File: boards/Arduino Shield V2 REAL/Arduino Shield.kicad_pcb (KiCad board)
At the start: 2 copper layers, 115 x 75 mm, 22 parts, among them J1 Screw_Terminal_01x07, J11 Screw_Terminal_01x08, J2 Screw_Terminal_01x08, J3 Screw_Terminal_01x08, J4 Screw_Terminal_01x08, J5 Screw_Terminal_01x08, J6 Screw_Terminal_01x08, J7 Screw_Terminal_01x08, J8 Screw_Terminal_01x07, J9 Screw_Terminal_01x10, U1 A000062

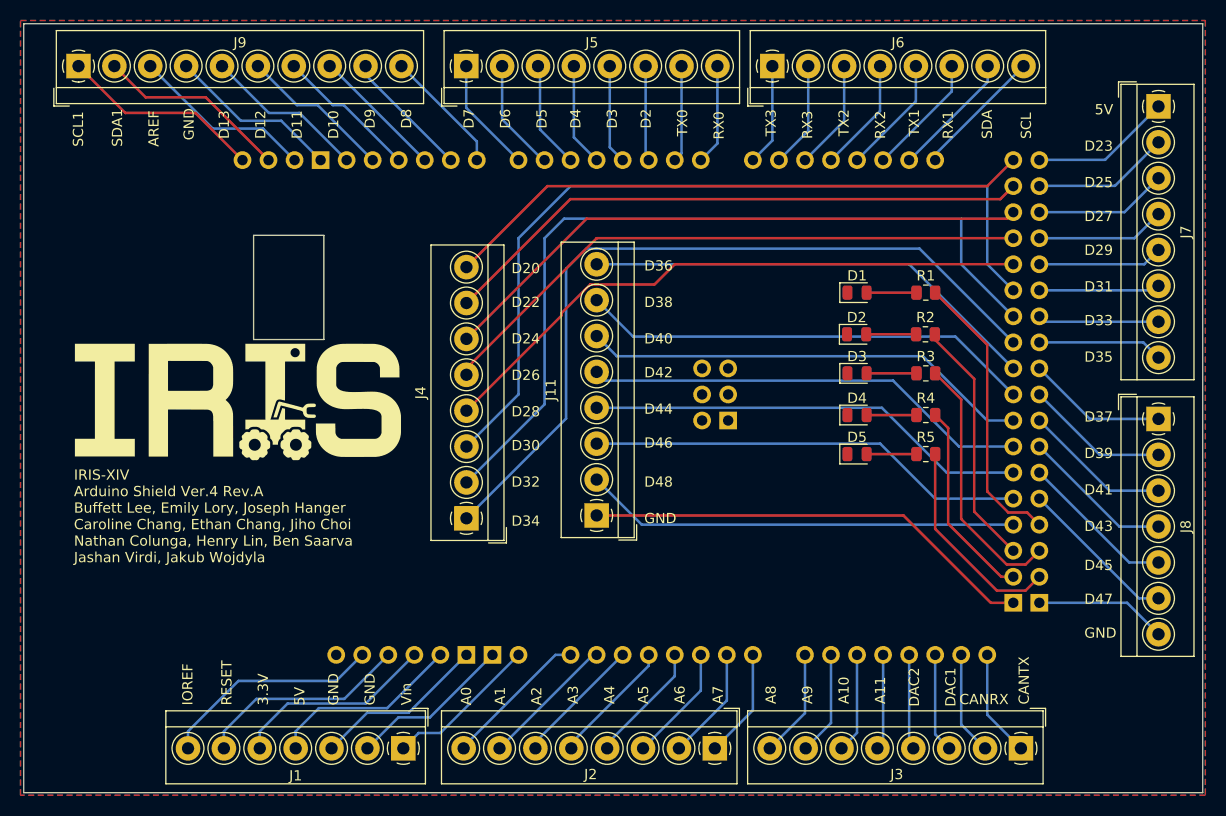
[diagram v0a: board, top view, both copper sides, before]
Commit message: Added LED labels and updated terminal block footprints
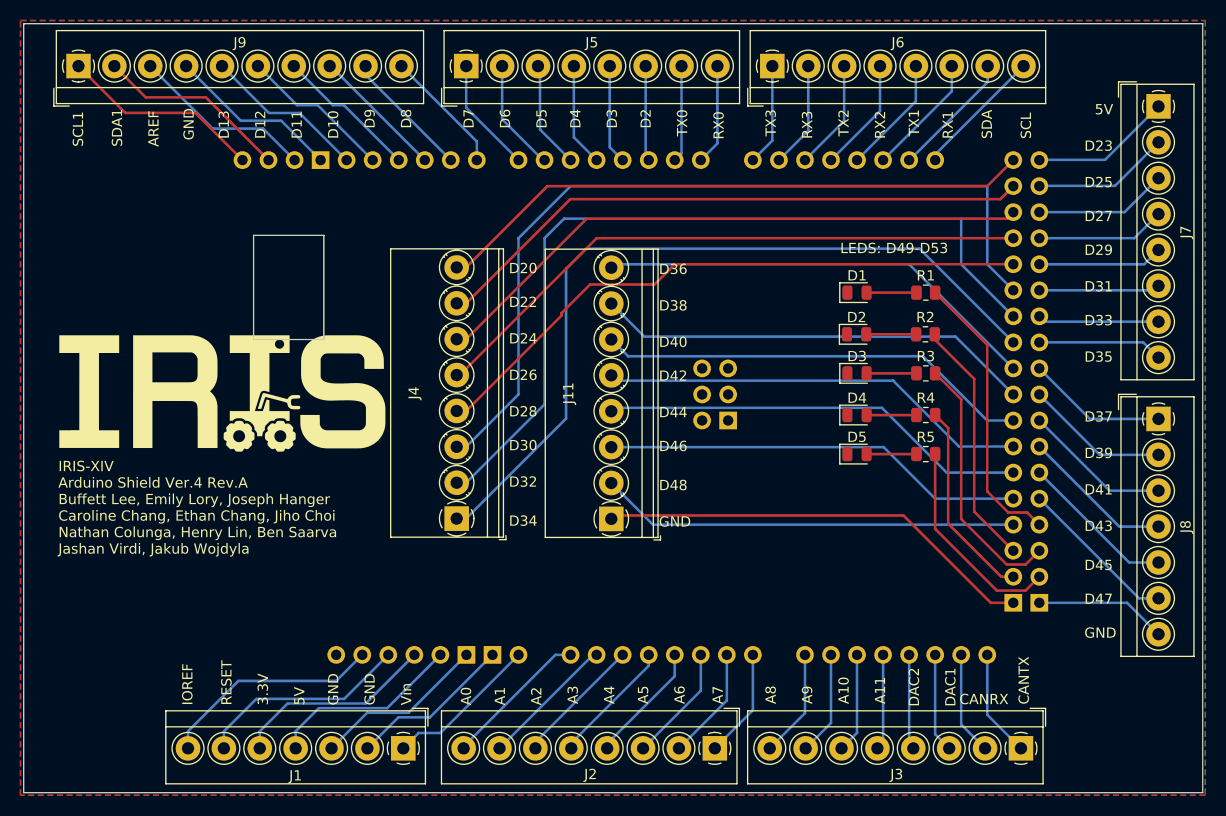
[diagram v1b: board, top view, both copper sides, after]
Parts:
- J11, J4: footprint TerminalBlock_4Ucon:TerminalBlock_4Ucon_1x08_P3.50mm_Horizontal -> TerminalBlock_Phoenix:TerminalBlock_Phoenix_PT-1,5-8-3.5-H_1x08_P3.50mm_Horizontal
- moved G*** 1.74 mm to (39.4, 55.9)
- moved J11 1.47 mm to (77.3, 68.3)
- moved J4 0.95 mm to (62.2, 68.3)
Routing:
- net Net-(J11-Pin_2): track 42.5 -> 40.9 mm
- net Net-(J11-Pin_6): track 44.1 -> 42.5 mm
- net Net-(J11-Pin_5): track 43.7 -> 42.1 mm
- net Net-(J11-Pin_3): track 42.9 -> 41.3 mm
- net Net-(J11-Pin_8): track 44.8 -> 43.6 mm
- net Net-(J11-Pin_4): track 43.3 -> 42.0 mm
- net GND: track 106.9 -> 105.6 mm
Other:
- board text added: "LEDS: D49-D53"
